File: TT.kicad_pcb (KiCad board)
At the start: 2 copper layers, 183 x 128.7 mm, 210 parts, among them J5 PI_ZERO, P1 CONN_02X05, Q1 Q_NPN_BEC, Q2 Q_NPN_BEC, Q3 Q_NPN_BEC, Q4 Q_NPN_BEC, SW1 SW_PUSH_SMALL_H, SW2 SW_PUSH_SMALL_H, SW3 SW_PUSH_SMALL_H, T1 JACK_QINGPU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

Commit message: corrected some values and the power inversion of U8
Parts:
- C20: value 56u -> 22u
- R11, R13, R2, R20, R26, R5: value 200k -> 100k
- R12, R14, R21, R27, R3, R6: value 100k -> 33k
- R30: value 13k -> 7k68
- R69, R70: value 100 -> 220
- U5: value AP2210N-3.3TRG1_/_SOT23-3 -> ~
- moved C42 13.0 mm to (51.8, 84.0), turned to 270 degrees
- moved C43 12.8 mm to (51.8, 71.0), turned to 270 degrees
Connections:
- U8 pad 11: +12V -> -12V
- U8 pad 4: -12V -> +12V
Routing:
- net +12V: track 164.7 -> 161.0 mm
- net -12V: track 62.9 -> 66.1 mm, vias 2 -> 4

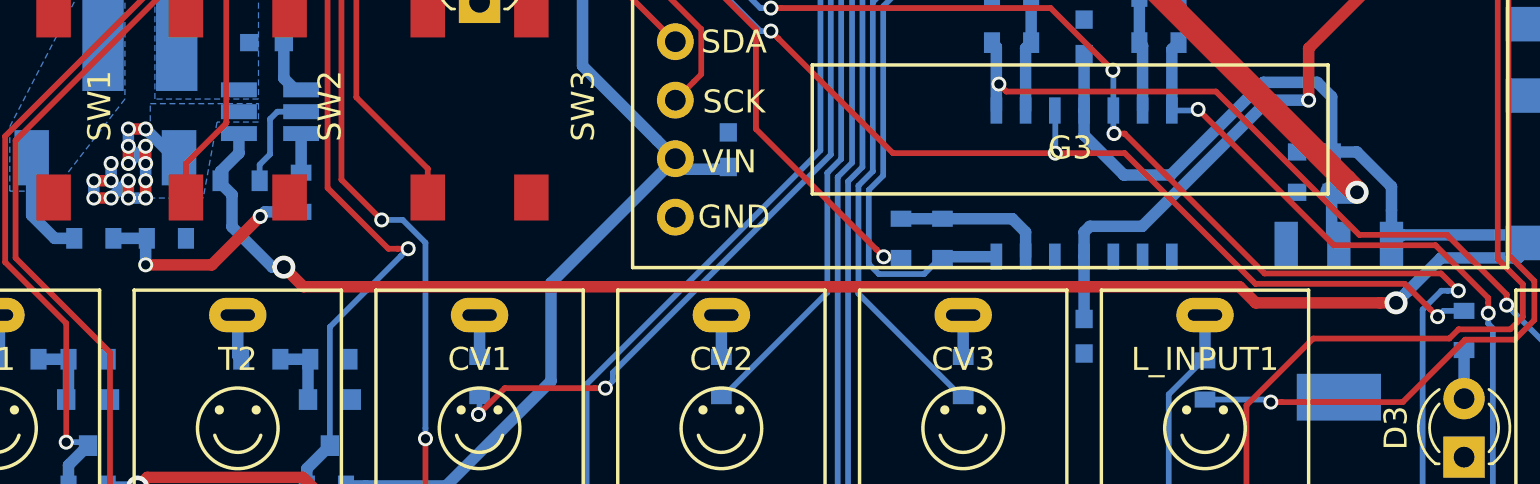
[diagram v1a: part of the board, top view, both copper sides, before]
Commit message: CV input stage values tweaked to original
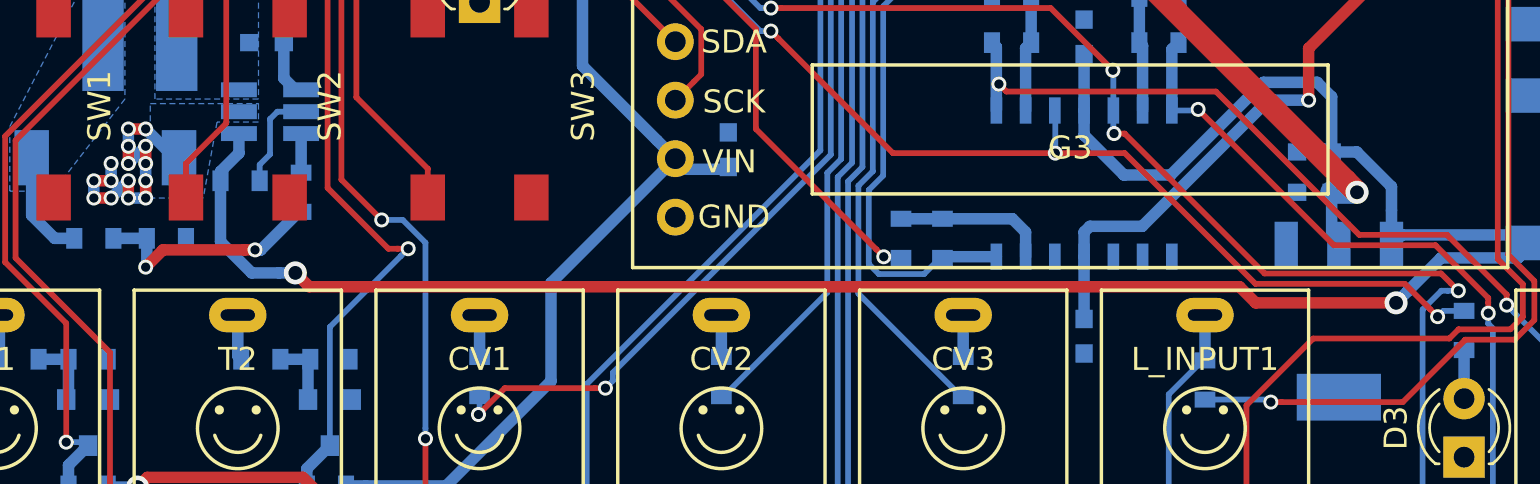
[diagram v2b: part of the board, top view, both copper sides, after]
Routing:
- net +12V: track 161.0 -> 161.7 mm
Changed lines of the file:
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@@
   (general
     (links 380)
-    (no_connects 3)
-    (area -93.100001 -10.450001 90.100001 118.450001)
+    (no_connects 0)
+    (area -106.100001 -14.9 98.595001 118.450001)
     (thickness 1.6)
     (drawings 1114)
-    (tracks 1452)
+    (tracks 1455)
     (zones 0)
     (modules 210)
@@
   )
   (setup
-    (last_trace_width 0.5)
+    (last_trace_width 0.25)
     (user_trace_width 0.25)
     (user_trace_width 0.5)
@@
   (segment (start 12.25 76.25) (end 11 75) (width 0.5) (layer B.Cu) (net 3))
   (via (at 11 75) (size 0.65) (drill 0.4) (layers F.Cu B.Cu) (net 3))
+  (segment (start 14.25 77.25) (end 14.25 79.897004) (width 0.5) (layer B.Cu) (net 4))
+  (segment (start 15.603006 81.25001) (end 16.792894 81.25001) (width 0.5) (layer B.Cu) (net 4))
+  (segment (start 14.25 79.897004) (end 15.603006 81.25001) (width 0.5) (layer B.Cu) (net 4))
+  (segment (start 16.792894 81.25001) (end 17.5 81.25001) (width 0.5) (layer B.Cu) (net 4))
+  (segment (start 17.999999 81.750009) (end 17.5 81.25001) (width 0.5) (layer F.Cu) (net 4))
+  (segment (start 18.101881 81.851891) (end 17.999999 81.750009) (width 0.5) (layer F.Cu) (net 4))
+  (segment (start 58.502293 81.851891) (end 18.101881 81.851891) (width 0.5) (layer F.Cu) (net 4))
+  (segment (start 65.296538 82.550022) (end 59.200424 82.550022) (width 0.5) (layer F.Cu) (net 4))
+  (segment (start 59.200424 82.550022) (end 58.502293 81.851891) (width 0.5) (layer F.Cu) (net 4))
+  (via (at 17.5 81.25001) (size 1) (drill 0.6) (layers F.Cu B.Cu) (net 4))
   (segment (start 51.75 75.2695) (end 51.75 74.198) (width 0.5) (layer B.Cu) (net 4))
   (segment (start 53.4805 77) (end 51.75 75.2695) (width 0.5) (layer B.Cu) (net 4))
@@
   (segment (start 62.5 73.602996) (end 61.872002 72.974998) (width 0.5) (layer B.Cu) (net 4))
   (segment (start 51.75 71.75) (end 51.75 74.198) (width 0.5) (layer B.Cu) (net 4))
-  (segment (start 17 81) (end 17.851891 81.851891) (width 0.5) (layer F.Cu) (net 4))
-  (segment (start 17.851891 81.851891) (end 58.502293 81.851891) (width 0.5) (layer F.Cu) (net 4))
-  (segment (start 58.502293 81.851891) (end 59.200424 82.550022) (width 0.5) (layer F.Cu) (net 4))
-  (segment (start 59.200424 82.550022) (end 64.589432 82.550022) (width 0.5) (layer F.Cu) (net 4))
-  (segment (start 64.589432 82.550022) (end 65.296538 82.550022) (width 0.5) (layer F.Cu) (net 4))
   (segment (start 71.25 79.95) (end 70.85 79.55) (width 0.5) (layer B.Cu) (net 4))
   (segment (start 71.25 79.95) (end 70.6 80.6) (width 0.5) (layer B.Cu) (net 4))
@@
   (segment (start 74.65 80) (end 71.3 80) (width 0.5) (layer B.Cu) (net 4))
   (segment (start 71.3 80) (end 71.25 79.95) (width 0.5) (layer B.Cu) (net 4))
-  (segment (start 14.75 79.25) (end 16.5 81) (width 0.5) (layer B.Cu) (net 4))
-  (segment (start 16.5 81) (end 17 81) (width 0.5) (layer B.Cu) (net 4))
-  (via (at 17 81) (size 1) (drill 0.6) (layers F.Cu B.Cu) (net 4))
-  (segment (start 14.75 77.85) (end 14.75 79.25) (width 0.5) (layer B.Cu) (net 4))
-  (segment (start 14.25 77.25) (end 14.25 77.35) (width 0.5) (layer B.Cu) (net 4))
-  (segment (start 14.25 77.35) (end 14.75 77.85) (width 0.5) (layer B.Cu) (net 4))
   (segment (start 15.05 75.2) (end 15.05 76.05) (width 0.5) (layer B.Cu) (net 4))
   (segment (start 15.05 76.05) (end 14.25 76.85) (width 0.5) (layer B.Cu) (net 4))
@@
   (segment (start 71.4 53.85) (end 71.5 53.75) (width 0.5) (layer B.Cu) (net 61))
   (segment (start 81.5 16.9) (end 81.5 14.75) (width 0.25) (layer B.Cu) (net 62))
+  (segment (start 17.75 74.25) (end 16.72 74.25) (width 0.25) (layer B.Cu) (net 63))
+  (segment (start 16.72 74.25) (end 16.4 74.57) (width 0.25) (layer B.Cu) (net 63))
   (segment (start 16.4 74.57) (end 16.4 76.1) (width 0.25) (layer B.Cu) (net 63))
   (segment (start 16.4 76.1) (end 15.95 76.55) (width 0.25) (layer B.Cu) (net 63))
   (segment (start 15.95 76.55) (end 15.95 77.25) (width 0.25) (layer B.Cu) (net 63))
-  (segment (start 17.75 74.25) (end 16.72 74.25) (width 0.25) (layer B.Cu) (net 63))
-  (segment (start 16.72 74.25) (end 16.4 74.57) (width 0.25) (layer B.Cu) (net 63))
   (segment (start 17.75 75.2) (end 17.75 76.9) (width 0.5) (layer B.Cu) (net 64))
-  (segment (start 11 80.9) (end 11 79.8) (width 0.5) (layer B.Cu) (net 65))
-  (segment (start 11 79.8) (end 11.05 79.75) (width 0.5) (layer B.Cu) (net 65))
-  (segment (start 15.974998 78.8) (end 13.874998 80.9) (width 0.5) (layer F.Cu) (net 65))
-  (via (at 11 80.9) (size 0.65) (drill 0.4) (layers F.Cu B.Cu) (net 65))
-  (segment (start 13.874998 80.9) (end 11 80.9) (width 0.5) (layer F.Cu) (net 65))
-  (segment (start 17.75 78.6) (end 16.174998 78.6) (width 0.5) (layer B.Cu) (net 65))
-  (segment (start 16.174998 78.6) (end 15.974998 78.8) (width 0.5) (layer B.Cu) (net 65))
-  (via (at 15.974998 78.8) (size 0.65) (drill 0.4) (layers F.Cu B.Cu) (net 65))
+  (segment (start 11.75 80.25) (end 15.290381 80.25) (width 0.5) (layer F.Cu) (net 65))
+  (segment (start 11 81) (end 11.75 80.25) (width 0.5) (layer F.Cu) (net 65))
+  (segment (start 17.75 78.6) (end 17.65 78.6) (width 0.5) (layer B.Cu) (net 65))
+  (segment (start 15.75001 80.25001) (end 15.75 80.25) (width 0.5) (layer B.Cu) (net 65))
+  (segment (start 16 80.25001) (end 15.75001 80.25001) (width 0.5) (layer B.Cu) (net 65))
+  (segment (start 16 80.25) (end 15.75 80.25) (width 0.5) (layer B.Cu) (net 65))
+  (segment (start 17.65 78.6) (end 16 80.25) (width 0.5) (layer B.Cu) (net 65))
+  (segment (start 15.290381 80.25) (end 15.75 80.25) (width 0.5) (layer F.Cu) (net 65))
+  (via (at 15.75 80.25) (size 0.65) (drill 0.4) (layers F.Cu B.Cu) (net 65))
+  (segment (start 11.05 80.95) (end 11 81) (width 0.5) (layer B.Cu) (net 65))
+  (segment (start 11.05 79.75) (end 11.05 80.95) (width 0.5) (layer B.Cu) (net 65))
+  (via (at 11 81) (size 0.65) (drill 0.4) (layers F.Cu B.Cu) (net 65))
   (segment (start 9.6 79.75) (end 11.05 79.75) (width 0.5) (layer B.Cu) (net 65))
   (segment (start 39.5 61.6) (end 39.5 63.75) (width 0.5) (layer B.Cu) (net 66))
